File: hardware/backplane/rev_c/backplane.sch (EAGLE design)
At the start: 357 parts, among them J0 BACKPLANE_GENERIC_MODULE, J1 BACKPLANE_GENERIC_MODULE, J2 BACKPLANE_GENERIC_MODULE, J3 BACKPLANE_CONTROLLER_MODULE, J4 BACKPLANE_POWER_MODULE, J5 BACKPLANE_GENERIC_MODULE, J6 BACKPLANE_GENERIC_MODULE, J7 BACKPLANE_GENERIC_MODULE, U1 TUSB2077A, U10 SN74LVC2T45, U11 SN74LVC2T45, U12 SN74LVC2T45, U13 SN74LVC2T45, U14 SN74LVC2T45, U15 SN74LVC2T45, U16 SN74LVC2T45, U17 SN74LVC2T45, U18 SN74LVC2T45, U19 SN74LVC2T45, U2 FXMA2102, U20 TS3USB30E, U21 TS3USB30E, U22 TS3USB30E, U23 TS3USB30E, U24 TS3USB30E, U25 TS3USB30E, U26 MCP23008, U27 MCP23008, U28 MCP23008, U29 MCP23008, U3 FXMA2102, U30 MCP23008, U31 MCP23008, U4 FXMA2102, U5 FXMA2102, U6 FXMA2102, U7 FXMA2102, U8 SN74LVC2T45, U9 SN74LVC2T45, Y1 ABMM

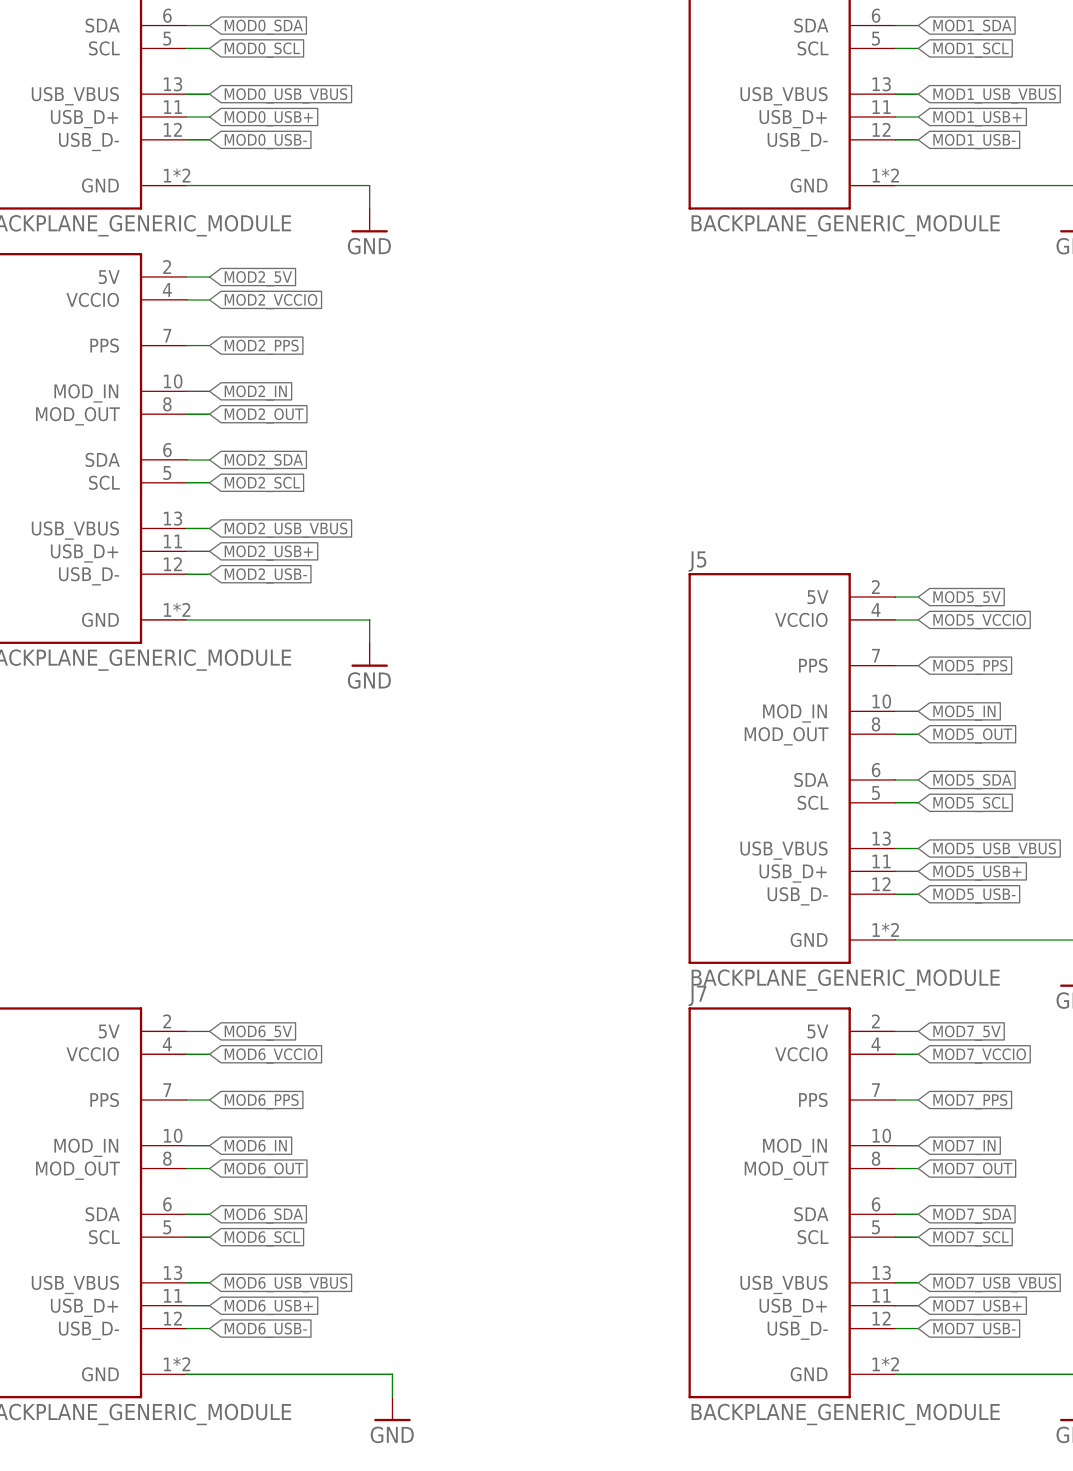
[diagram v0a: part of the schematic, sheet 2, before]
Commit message: backplane: update modules to have plated holes
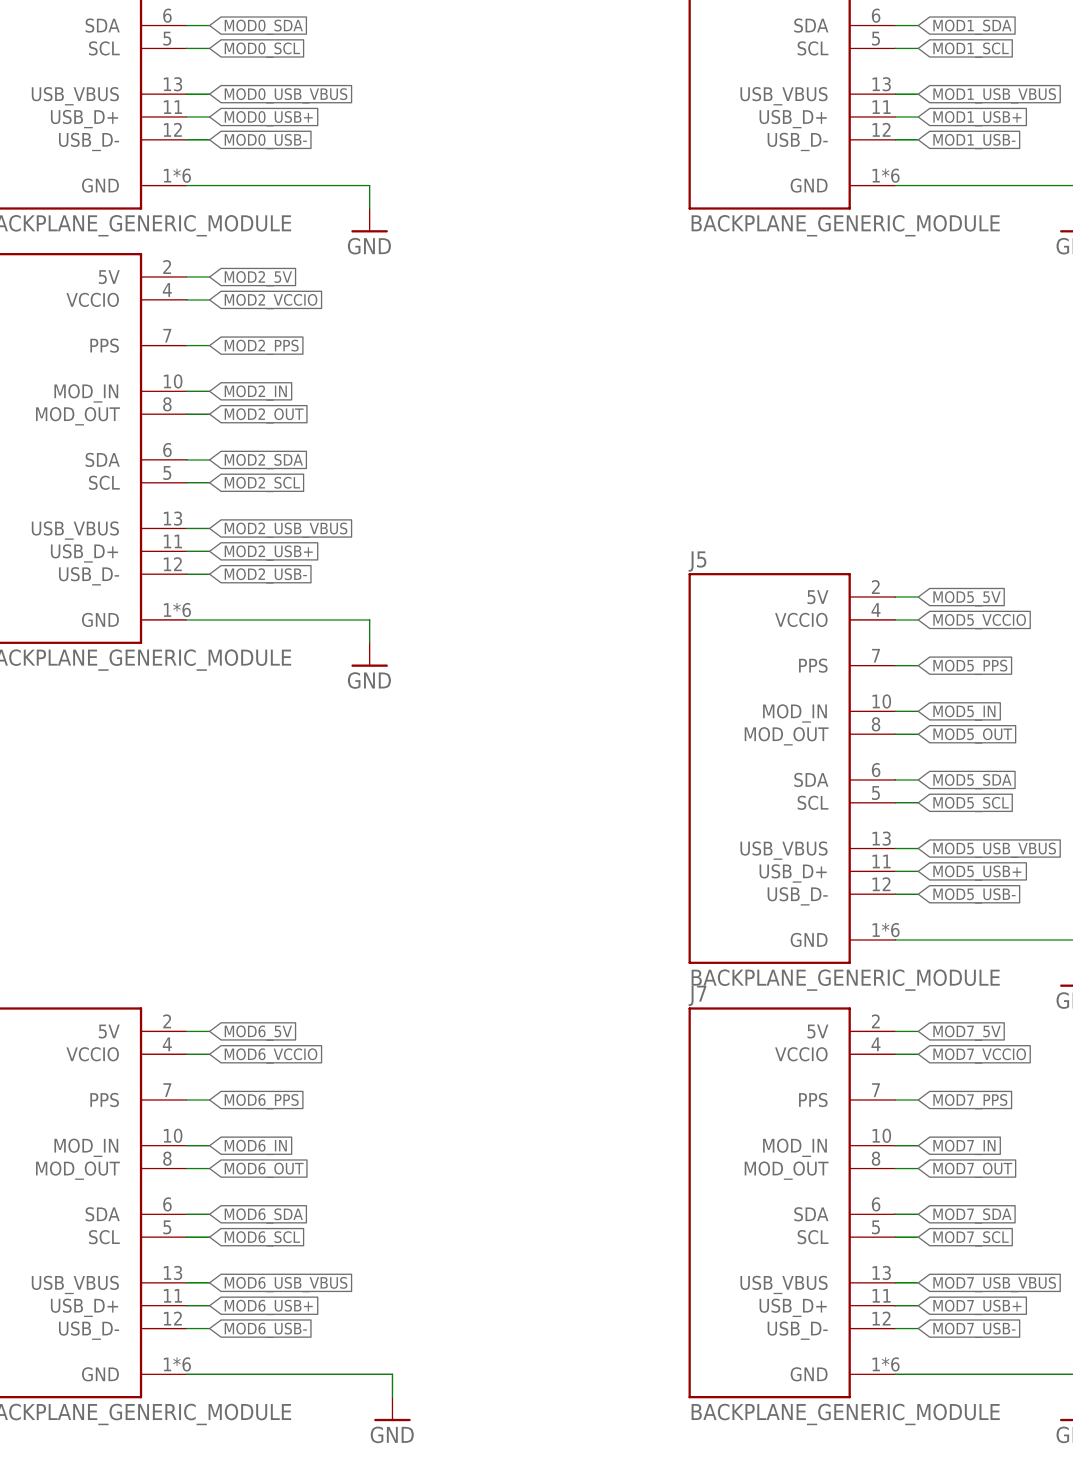
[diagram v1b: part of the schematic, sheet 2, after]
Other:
- moved on the sheet: J4
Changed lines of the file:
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@@
 <layer number="57" name="tCAD" color="7" fill="1" visible="no" active="no"/>
 <layer number="59" name="Invisible" color="7" fill="1" visible="no" active="no"/>
+<layer number="60" name="bCarbon" color="7" fill="1" visible="no" active="no"/>
 <layer number="61" name="stand" color="7" fill="1" visible="no" active="no"/>
+<layer number="90" name="Modules" color="5" fill="1" visible="no" active="no"/>
 <layer number="91" name="Nets" color="2" fill="1" visible="yes" active="yes"/>
 <layer number="92" name="Busses" color="1" fill="1" visible="yes" active="yes"/>
@@
 <layer number="113" name="IDFDebug" color="7" fill="1" visible="no" active="yes"/>
 <layer number="116" name="Patch_BOT" color="9" fill="4" visible="no" active="yes"/>
+<layer number="118" name="Rect_Pads" color="7" fill="1" visible="yes" active="yes"/>
 <layer number="121" name="_tsilk" color="7" fill="1" visible="no" active="yes"/>
 <layer number="122" name="_bsilk" color="7" fill="1" visible="no" active="yes"/>
@@
 <layer number="127" name="_tValues" color="7" fill="1" visible="no" active="yes"/>
 <layer number="128" name="_bValues" color="7" fill="1" visible="no" active="yes"/>
+<layer number="129" name="Mask" color="7" fill="1" visible="yes" active="yes"/>
 <layer number="130" name="bLogo" color="7" fill="1" visible="yes" active="yes"/>
 <layer number="131" name="tAdjust" color="7" fill="1" visible="yes" active="yes"/>
@@
 <layer number="223" name="223bmp" color="24" fill="1" visible="no" active="no"/>
 <layer number="224" name="224bmp" color="25" fill="1" visible="no" active="no"/>
+<layer number="225" name="225bmp" color="7" fill="1" visible="yes" active="yes"/>
+<layer number="226" name="226bmp" color="7" fill="1" visible="yes" active="yes"/>
+<layer number="227" name="227bmp" color="7" fill="1" visible="yes" active="yes"/>
+<layer number="228" name="228bmp" color="7" fill="1" visible="yes" active="yes"/>
+<layer number="229" name="229bmp" color="7" fill="1" visible="yes" active="yes"/>
+<layer number="230" name="230bmp" color="7" fill="1" visible="yes" active="yes"/>
 <layer number="231" name="Eagle3D_PG1" color="14" fill="1" visible="yes" active="yes"/>
 <layer number="232" name="Eagle3D_PG2" color="14" fill="2" visible="yes" active="yes"/>
@@
 <layer number="251" name="SMDround" color="12" fill="11" visible="no" active="no"/>
 <layer number="254" name="cooling" color="7" fill="1" visible="no" active="yes"/>
+<layer number="255" name="routoute" color="7" fill="1" visible="yes" active="yes"/>
 </layers>
 <schematic xreflabel="%F%N/%S.%C%R" xrefpart="/%S.%C%R">

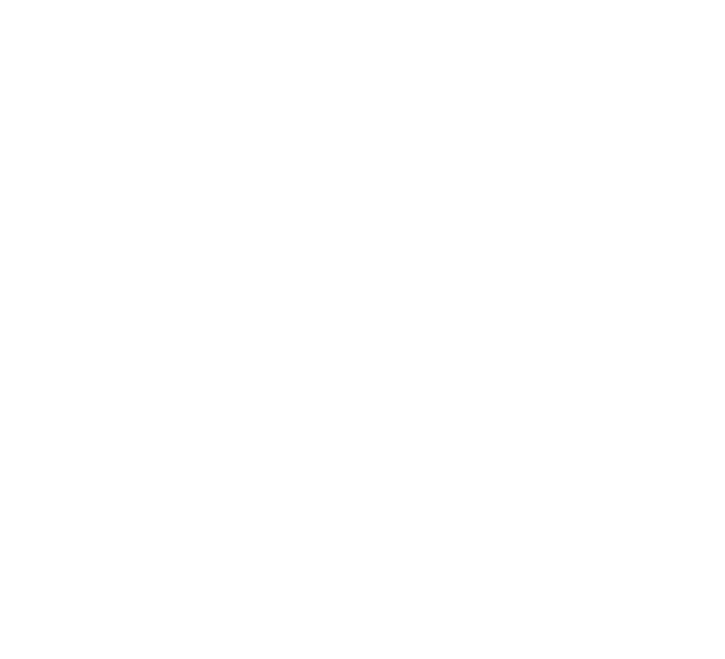
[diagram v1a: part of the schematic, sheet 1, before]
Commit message: backplane: plated board mounting holes
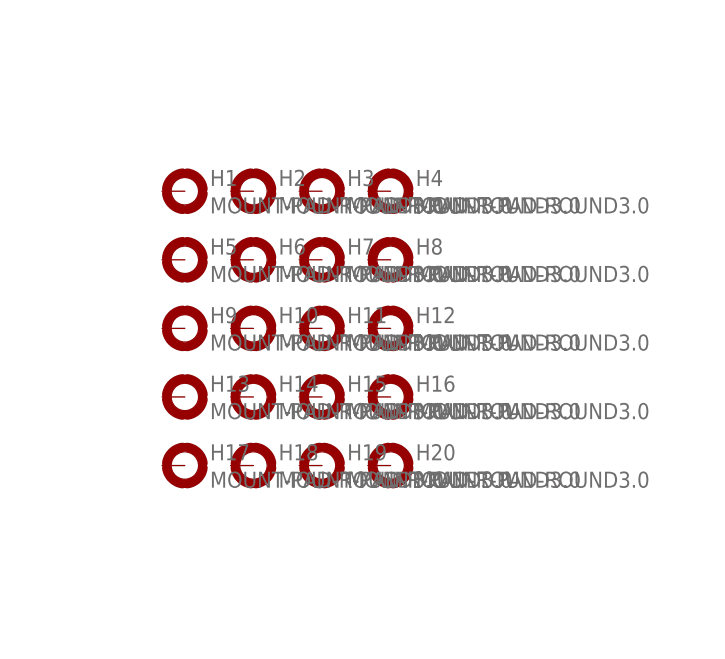
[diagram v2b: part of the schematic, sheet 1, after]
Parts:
- added H1, H10, H11, H12, H13, H14, H15, H16, H17, H18, H19, H2, H20, H3, H4, H5, H6, H7, H8, H9: MOUNT-PAD-ROUND3.0, holes:MOUNT-PAD-ROUND3.0
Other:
- note added: "Plated Mounting Holes"
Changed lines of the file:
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@@
 <part name="JP5" library="SparkFun-Aesthetics" deviceset="FIDUCIAL" device="1X2"/>
 <part name="JP6" library="SparkFun-Aesthetics" deviceset="FIDUCIAL" device="1X2"/>
+<part name="H1" library="holes" deviceset="MOUNT-PAD-ROUND" device="3.0"/>
+<part name="H2" library="holes" deviceset="MOUNT-PAD-ROUND" device="3.0"/>
+<part name="H3" library="holes" deviceset="MOUNT-PAD-ROUND" device="3.0"/>
+<part name="H4" library="holes" deviceset="MOUNT-PAD-ROUND" device="3.0"/>
+<part name="H5" library="holes" deviceset="MOUNT-PAD-ROUND" device="3.0"/>
+<part name="H6" library="holes" deviceset="MOUNT-PAD-ROUND" device="3.0"/>
+<part name="H7" library="holes" deviceset="MOUNT-PAD-ROUND" device="3.0"/>
+<part name="H8" library="holes" deviceset="MOUNT-PAD-ROUND" device="3.0"/>
+<part name="H9" library="holes" deviceset="MOUNT-PAD-ROUND" device="3.0"/>
+<part name="H10" library="holes" deviceset="MOUNT-PAD-ROUND" device="3.0"/>
+<part name="H11" library="holes" deviceset="MOUNT-PAD-ROUND" device="3.0"/>
+<part name="H12" library="holes" deviceset="MOUNT-PAD-ROUND" device="3.0"/>
+<part name="H13" library="holes" deviceset="MOUNT-PAD-ROUND" device="3.0"/>
+<part name="H14" library="holes" deviceset="MOUNT-PAD-ROUND" device="3.0"/>
+<part name="H15" library="holes" deviceset="MOUNT-PAD-ROUND" device="3.0"/>
+<part name="H16" library="holes" deviceset="MOUNT-PAD-ROUND" device="3.0"/>
+<part name="H17" library="holes" deviceset="MOUNT-PAD-ROUND" device="3.0"/>
+<part name="H18" library="holes" deviceset="MOUNT-PAD-ROUND" device="3.0"/>
+<part name="H19" library="holes" deviceset="MOUNT-PAD-ROUND" device="3.0"/>
+<part name="H20" library="holes" deviceset="MOUNT-PAD-ROUND" device="3.0"/>
 </parts>
 <sheets>
@@
 <wire x1="203.2" y1="76.2" x2="203.2" y2="20.32" width="0.6096" layer="98"/>
 <text x="220.98" y="71.12" size="2.54" layer="98" align="center">Fiducials</text>
+<wire x1="203.2" y1="132.08" x2="203.2" y2="76.2" width="0.6096" layer="98"/>
+<text x="223.52" y="129.54" size="2.54" layer="98" align="center">Plated Mounting Holes</text>
 </plain>
 <instances>
@@
 <instance part="JP5" gate="G$1" x="215.9" y="40.64"/>
 <instance part="JP6" gate="G$1" x="223.52" y="40.64"/>
+<instance part="H1" gate="G$1" x="208.28" y="121.92"/>
+<instance part="H2" gate="G$1" x="215.9" y="121.92"/>
+<instance part="H3" gate="G$1" x="223.52" y="121.92"/>
+<instance part="H4" gate="G$1" x="231.14" y="121.92"/>
+<instance part="H5" gate="G$1" x="208.28" y="114.3"/>
+<instance part="H6" gate="G$1" x="215.9" y="114.3"/>
+<instance part="H7" gate="G$1" x="223.52" y="114.3"/>
+<instance part="H8" gate="G$1" x="231.14" y="114.3"/>
+<instance part="H9" gate="G$1" x="208.28" y="106.68"/>
+<instance part="H10" gate="G$1" x="215.9" y="106.68"/>
+<instance part="H11" gate="G$1" x="223.52" y="106.68"/>
+<instance part="H12" gate="G$1" x="231.14" y="106.68"/>
+<instance part="H13" gate="G$1" x="208.28" y="99.06"/>
+<instance part="H14" gate="G$1" x="215.9" y="99.06"/>
+<instance part="H15" gate="G$1" x="223.52" y="99.06"/>
+<instance part="H16" gate="G$1" x="231.14" y="99.06"/>
+<instance part="H17" gate="G$1" x="208.28" y="91.44"/>
+<instance part="H18" gate="G$1" x="215.9" y="91.44"/>
+<instance part="H19" gate="G$1" x="223.52" y="91.44"/>
+<instance part="H20" gate="G$1" x="231.14" y="91.44"/>
 </instances>
 <busses>
